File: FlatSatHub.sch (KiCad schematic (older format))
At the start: 5 parts, among them J1 Jack-DC

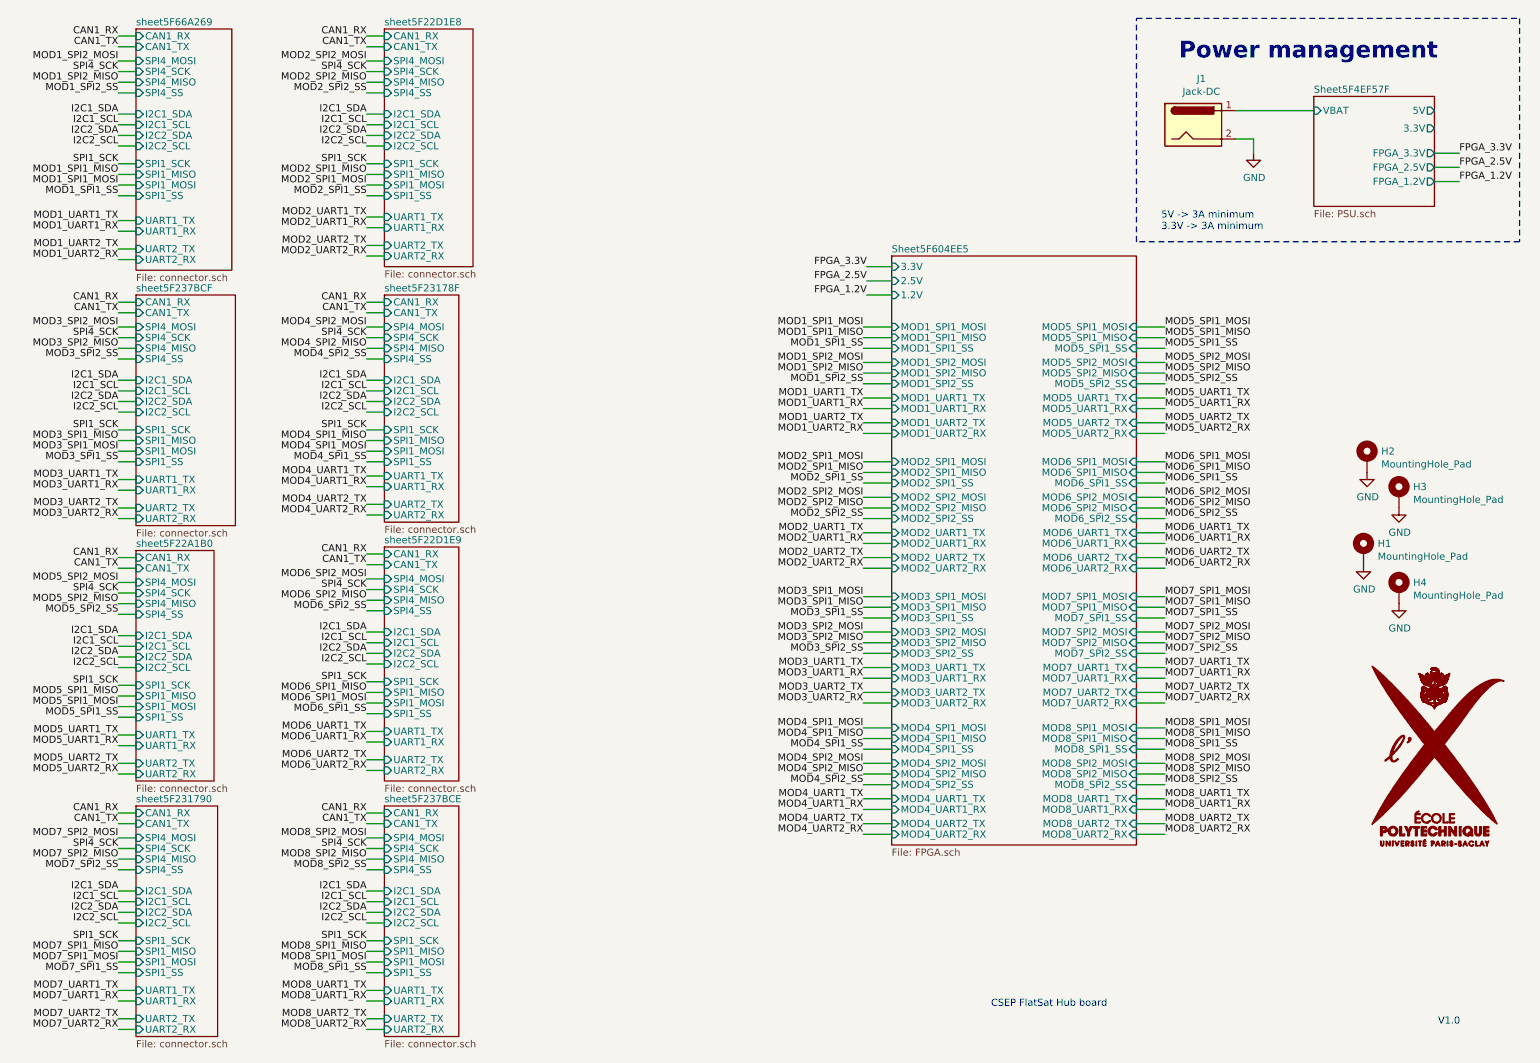
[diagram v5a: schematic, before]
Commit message: Most PSB done, needs more silk screen cosmetic plus review
Signed-off-by: Alexis Jeandet <alexis.jeandet@member.fsf.org>
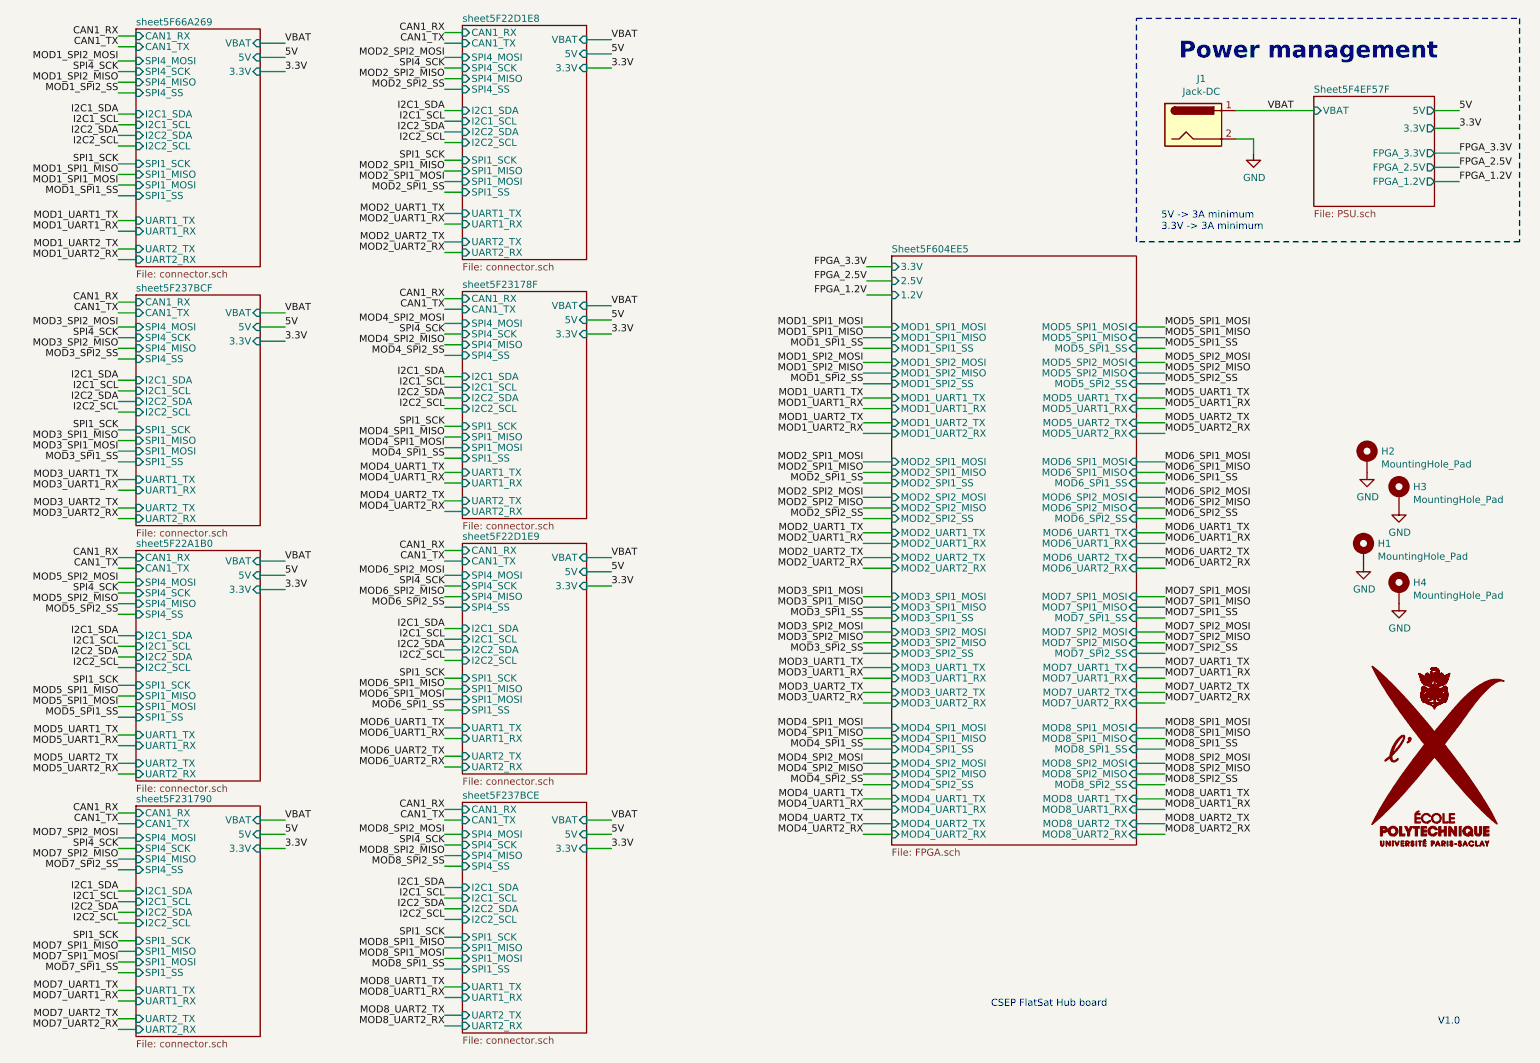
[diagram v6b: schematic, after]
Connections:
- net Sheet5F4EF57F/VBAT renamed VBAT
